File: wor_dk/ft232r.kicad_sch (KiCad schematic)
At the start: 18 parts, among them J401 USB_C_Receptacle_USB2.0_14P, U401 FT232RL

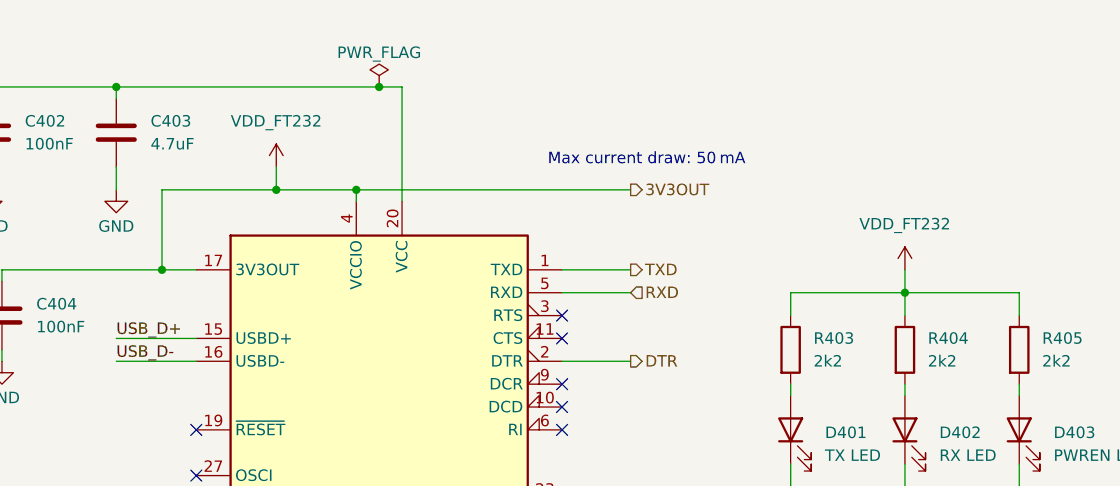
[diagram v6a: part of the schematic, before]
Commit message: wor_dk: top-level connections & cleanup
- top-level connections for TMUX control & UART done (selection
  between FTDI and DAP Link via jumpers)
- all ERC errors & warnings cleaned up
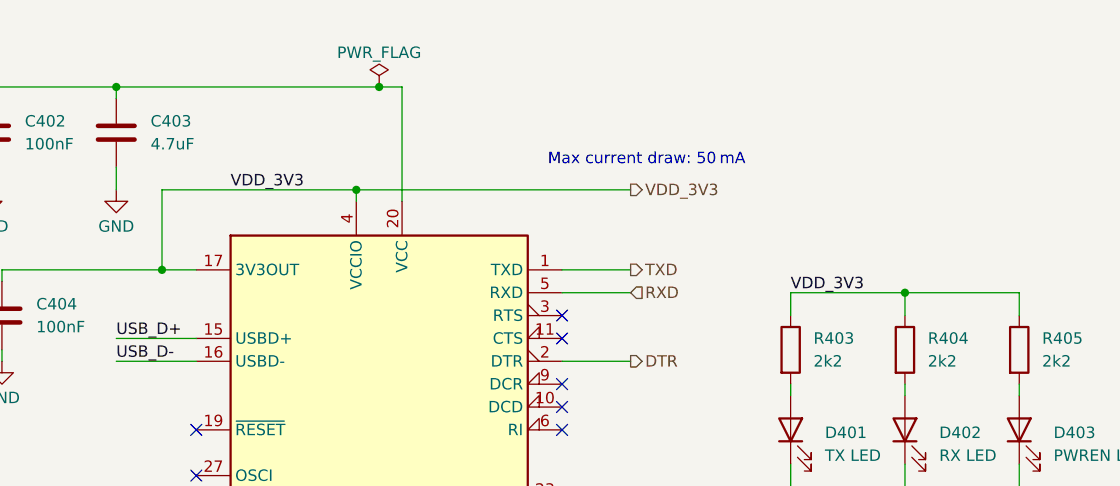
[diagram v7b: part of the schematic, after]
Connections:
- net VDD_FT232 renamed VDD_3V3
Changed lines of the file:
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@@
 	)
 	(junction
-		(at 185.42 72.39)
-		(diameter 0)
-		(color 0 0 0 0)
-	)
-	(junction
 		(at 172.72 81.28)
 		(diameter 0)
@@
 	(wire
 		(pts
-			(xy 255.27 81.28) (xy 255.27 83.82)
-		)
-		(stroke
-			(width 0)
-			(type default)
-		)
-	)
-	(wire
-		(pts
 			(xy 50.8 128.27) (xy 58.42 128.27)
 		)
@@
 	(wire
 		(pts
-			(xy 185.42 72.39) (xy 172.72 72.39)
+			(xy 172.72 72.39) (xy 194.31 72.39)
 		)
 		(stroke
@@
 	(wire
 		(pts
-			(xy 185.42 69.85) (xy 185.42 72.39)
-		)
-		(stroke
-			(width 0)
-			(type default)
-		)
-	)
-	(wire
-		(pts
 			(xy 198.12 127) (xy 198.12 129.54)
 		)
@@
 	(wire
 		(pts
-			(xy 194.31 72.39) (xy 185.42 72.39)
-		)
-		(stroke
-			(width 0)
-			(type default)
-		)
-	)
-	(wire
-		(pts
 			(xy 93.98 83.82) (xy 93.98 87.63)
 		)
@@
 		)
 	)
+	(label "VDD_3V3"
+		(at 180.34 72.39 0)
+		(fields_autoplaced yes)
+		(effects
+			(font
+				(size 1.27 1.27)
+			)
+			(justify left bottom)
+		)
+	)
 	(label "USB_D+"
 		(at 167.64 88.9 0)
@@
 		)
 	)
+	(label "VDD_3V3"
+		(at 242.57 83.82 0)
+		(fields_autoplaced yes)
+		(effects
+			(font
+				(size 1.27 1.27)
+			)
+			(justify left bottom)
+		)
+	)
 	(label "USB_D+"
 		(at 77.47 96.52 0)
@@
 		)
 	)
-	(hierarchical_label "3V3OUT"
+	(hierarchical_label "VDD_3V3"
 		(shape output)
 		(at 224.79 72.39 0)
@@
 	)
 	(symbol
-		(lib_id "power:VDD")
-		(at 255.27 81.28 0)
-		(unit 1)
-		(exclude_from_sim no)
-		(in_bom yes)
-		(on_board yes)
-		(dnp no)
-		(fields_autoplaced yes)
-		(property "Reference" "#PWR0405"
-			(at 255.27 85.09 0)
-			(effects
-				(font
-					(size 1.27 1.27)
-				)
-				(hide yes)
-			)
-		)
-		(property "Value" "VDD_FT232"
-			(at 255.27 76.2 0)
-			(effects
-				(font
-					(size 1.27 1.27)
-				)
-			)
-		)
-		(property "Footprint" ""
-			(at 255.27 81.28 0)
-			(effects
-				(font
-					(size 1.27 1.27)
-				)
-				(hide yes)
-			)
-		)
-		(property "Datasheet" ""
-			(at 255.27 81.28 0)
-			(effects
-				(font
-					(size 1.27 1.27)
-				)
-				(hide yes)
-			)
-		)
-		(property "Description" "Power symbol creates a global label with name \"VDD\""
-			(at 255.27 81.28 0)
-			(effects
-				(font
-					(size 1.27 1.27)
-				)
-				(hide yes)
-			)
-		)
-		(pin "1"
-		)
-		(instances
-			(project ""
-				(path "/8d3147eb-060b-4f65-bf42-ed06a58b21ba/711499aa-b4ff-4669-a7c0-a5db1aab8120"
-					(reference "#PWR0405")
-					(unit 1)
-				)
-			)
-		)
-	)
-	(symbol
 		(lib_id "power:GND")
 		(at 154.94 91.44 0)
@@
 					(unit 1)
 				)
-			)
-		)
-	)
-	(symbol
-		(lib_id "power:VDD")
-		(at 185.42 69.85 0)
-		(unit 1)
-		(exclude_from_sim no)
-		(in_bom yes)
-		(on_board yes)
-		(dnp no)
-		(fields_autoplaced yes)
-		(property "Reference" "#PWR0401"
-			(at 185.42 73.66 0)
-			(effects
-				(font
-					(size 1.27 1.27)
-				)
-				(hide yes)
-			)
-		)
-		(property "Value" "VDD_FT232"
-			(at 185.42 64.77 0)
-			(effects
-				(font
-					(size 1.27 1.27)
-				)
-			)
-		)
-		(property "Footprint" ""
-			(at 185.42 69.85 0)
-			(effects
-				(font
-					(size 1.27 1.27)
-				)
-				(hide yes)
-			)
-		)
-		(property "Datasheet" ""
-			(at 185.42 69.85 0)
-			(effects
-				(font
-					(size 1.27 1.27)
-				)
-				(hide yes)
-			)
-		)
-		(property "Description" "Power symbol creates a global label with name \"VDD\""
-			(at 185.42 69.85 0)
-			(effects
-				(font
-					(size 1.27 1.27)
-				)
-				(hide yes)
-			)
-		)
-		(pin "1"
-		)
-		(instances
-			(project "wor_dk"
-				(path "/8d3147eb-060b-4f65-bf42-ed06a58b21ba/711499aa-b4ff-4669-a7c0-a5db1aab8120"
-					(reference "#PWR0401")
-					(unit 1)
-				)

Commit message: wor_dk: add footprints & part info for all resistors
All resistors are JLCPCB basic parts. Footprint 0402 is used for all
resistors, except for 0 Ω resistors, where 0805 is used.
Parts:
- R401, R402: footprint (none) -> Resistor_SMD:R_0402_1005Metric; Comment (none) -> JLCPCB basic part; LCSC (none) -> C25905; MPN (none) -> 0402WGF5101TCE; Manufacturer (none) -> Uniroyal Elec
- R403, R404, R405: MPN (none) -> 0402WGF2201TCE
- R406: footprint (none) -> Resistor_SMD:R_0805_2012Metric; Comment (none) -> JLCPCB basic part; LCSC (none) -> C17477; MPN (none) -> 0805W8F0000T5E; Manufacturer (none) -> Uniroyal Elec
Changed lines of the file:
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@@
 			)
 		)
-		(property "Footprint" ""
+		(property "Footprint" "Resistor_SMD:R_0805_2012Metric"
 			(at 49.022 120.65 90)
 			(effects
@@
 			)
 		)
-		(property "Datasheet" "~"
+		(property "Datasheet" "https://wmsc.lcsc.com/wmsc/upload/file/pdf/v2/lcsc/2206010216_UNI-ROYAL-Uniroyal-Elec-0805W8F0000T5E_C17477.pdf"
 			(at 50.8 120.65 0)
 			(effects
@@
 			)
 		)
-		(property "Description" "Resistor"
+		(property "Description" "25mW Thick Film Resistors 150V ±800ppm/℃ ±1% 0Ω 0805"
+			(at 50.8 120.65 0)
+			(effects
+				(font
+					(size 1.27 1.27)
+				)
+				(hide yes)
+			)
+		)
+		(property "Comment" "JLCPCB basic part"
+			(at 50.8 120.65 0)
+			(effects
+				(font
+					(size 1.27 1.27)
+				)
+				(hide yes)
+			)
+		)
+		(property "LCSC" "C17477"
+			(at 50.8 120.65 0)
+			(effects
+				(font
+					(size 1.27 1.27)
+				)
+				(hide yes)
+			)
+		)
+		(property "MPN" "0805W8F0000T5E"
+			(at 50.8 120.65 0)
+			(effects
+				(font
+					(size 1.27 1.27)
+				)
+				(hide yes)
+			)
+		)
+		(property "Manufacturer" "Uniroyal Elec"
 			(at 50.8 120.65 0)
 			(effects
@@
 			)
 		)
-		(property "Footprint" ""
+		(property "Footprint" "Resistor_SMD:R_0402_1005Metric"
 			(at 85.09 85.598 90)
 			(effects
@@
 			)
 		)
-		(property "Datasheet" "~"
+		(property "Datasheet" "https://wmsc.lcsc.com/wmsc/upload/file/pdf/v2/lcsc/2206010045_UNI-ROYAL-Uniroyal-Elec-0402WGF5101TCE_C25905.pdf"
 			(at 85.09 83.82 0)
 			(effects
@@
 			)
 		)
-		(property "Description" "Resistor"
+		(property "Description" "62.5mW Thick Film Resistors 50V ±100ppm/℃ ±1% 5.1kΩ 0402"
+			(at 85.09 83.82 0)
+			(effects
+				(font
+					(size 1.27 1.27)
+				)
+				(hide yes)
+			)
+		)
+		(property "LCSC" "C25905"
+			(at 85.09 83.82 0)
+			(effects
+				(font
+					(size 1.27 1.27)
+				)
+				(hide yes)
+			)
+		)
+		(property "MPN" "0402WGF5101TCE"
+			(at 85.09 83.82 0)
+			(effects
+				(font
+					(size 1.27 1.27)
+				)
+				(hide yes)
+			)
+		)
+		(property "Manufacturer" "Uniroyal Elec"
+			(at 85.09 83.82 0)
+			(effects
+				(font
+					(size 1.27 1.27)
+				)
+				(hide yes)
+			)
+		)
+		(property "Comment" "JLCPCB basic part"
 			(at 85.09 83.82 0)
 			(effects
@@
 			)
 		)
-		(property "Footprint" ""
+		(property "Footprint" "Resistor_SMD:R_0402_1005Metric"
 			(at 85.09 79.502 90)
 			(effects
@@
 			)
 		)
-		(property "Datasheet" "~"
+		(property "Datasheet" "https://wmsc.lcsc.com/wmsc/upload/file/pdf/v2/lcsc/2206010045_UNI-ROYAL-Uniroyal-Elec-0402WGF5101TCE_C25905.pdf"
 			(at 85.09 81.28 0)
 			(effects
@@
 			)
 		)
-		(property "Description" "Resistor"
+		(property "Description" "62.5mW Thick Film Resistors 50V ±100ppm/℃ ±1% 5.1kΩ 0402"
+			(at 85.09 81.28 0)
+			(effects
+				(font
+					(size 1.27 1.27)
+				)
+				(hide yes)
+			)
+		)
+		(property "LCSC" "C25905"
+			(at 85.09 81.28 0)
+			(effects
+				(font
+					(size 1.27 1.27)
+				)
+				(hide yes)
+			)
+		)
+		(property "MPN" "0402WGF5101TCE"
+			(at 85.09 81.28 0)
+			(effects
+				(font
+					(size 1.27 1.27)
+				)
+				(hide yes)
+			)
+		)
+		(property "Manufacturer" "Uniroyal Elec"
+			(at 85.09 81.28 0)
+			(effects
+				(font
+					(size 1.27 1.27)
+				)
+				(hide yes)
+			)
+		)
+		(property "Comment" "JLCPCB basic part"
 			(at 85.09 81.28 0)
 			(effects
@@
 			)
 		)
+		(property "MPN" "0402WGF2201TCE"
+			(at 267.97 90.17 0)
+			(effects
+				(font
+					(size 1.27 1.27)
+				)
+				(hide yes)
+			)
+		)
 		(pin "1"
 		)
@@
 			)
 		)
+		(property "MPN" "0402WGF2201TCE"
+			(at 242.57 90.17 0)
+			(effects
+				(font
+					(size 1.27 1.27)
+				)
+				(hide yes)
+			)
+		)
 		(pin "1"
 		)
@@
 			(at 255.27 90.17 0)
 			(effects
+				(font
+					(size 1.27 1.27)
+				)
+				(hide yes)
+			)
+		)
+		(property "MPN" "0402WGF2201TCE"
+			(at 255.27 90.17 0)
+			(effects
